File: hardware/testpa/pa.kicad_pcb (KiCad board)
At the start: 4 copper layers, 50 x 50 mm, 61 parts, among them CN1 CONN_01X02, J1 JNC, J2 JNC, Q1 LDMOS, Q2 LDMOS, T1 TRANSF4CTS, T2 1:1 Z, U1 LP2985

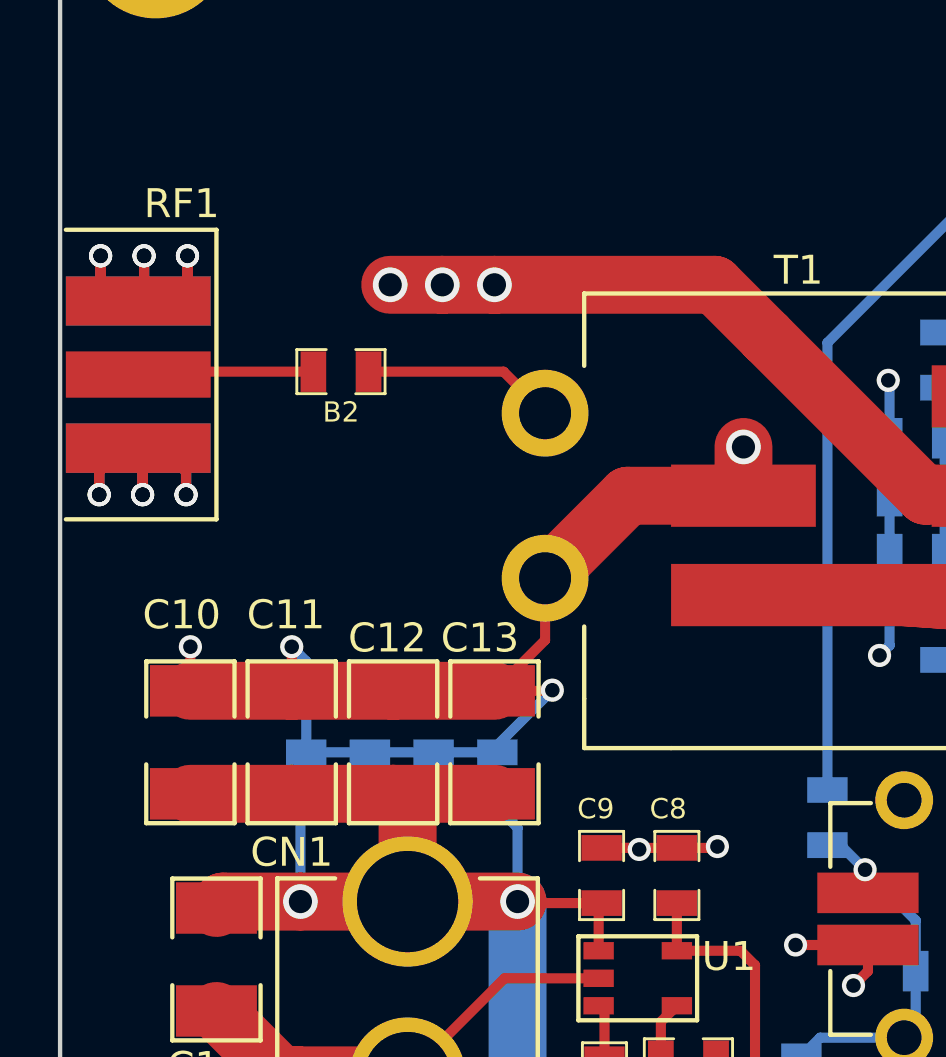
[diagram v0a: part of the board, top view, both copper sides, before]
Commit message: RF output fix on testpa
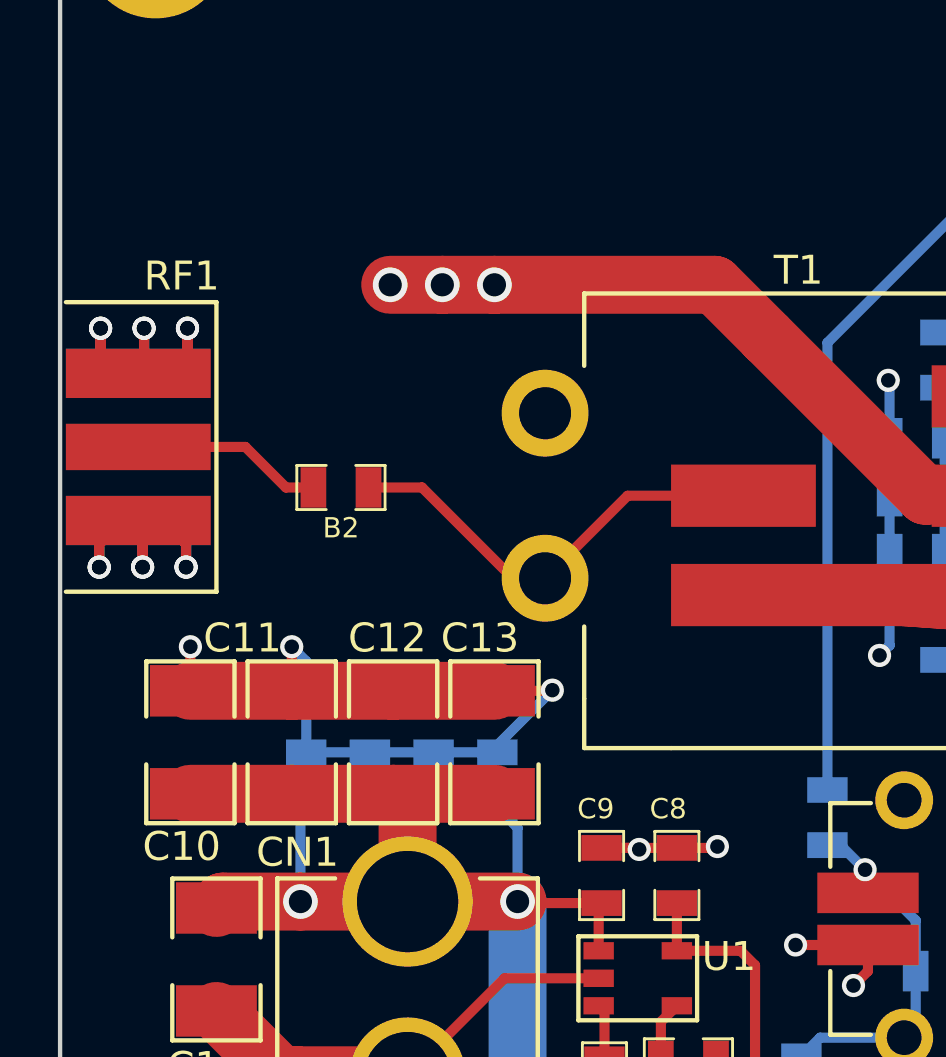
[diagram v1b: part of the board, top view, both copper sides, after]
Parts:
- moved B2 4.00 mm to (124.7, 97.0)
- moved RF1 2.50 mm to (115.0, 95.6)
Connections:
- T1 pad 4: Net-(B2-Pad2) -> GND
- T1 pad 5: GND -> Net-(B2-Pad2)
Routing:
- net GND: track 303.2 -> 288.6 mm, vias 57 -> 56
- net Net-(B2-Pad2): track 6.69 -> 15.4 mm
- net Net-(B2-Pad1): track 6.09 -> 6.63 mm

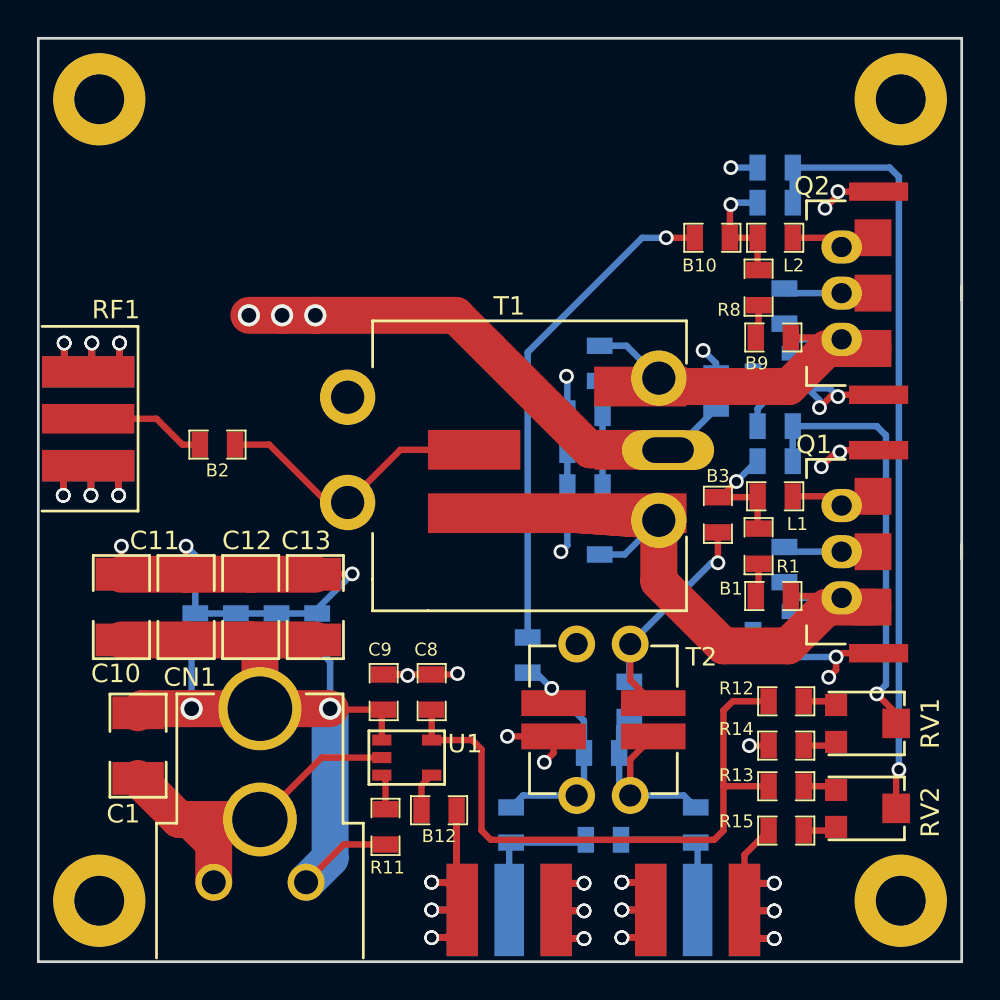
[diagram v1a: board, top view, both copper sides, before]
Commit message: Silk screen sizes, copyright notice
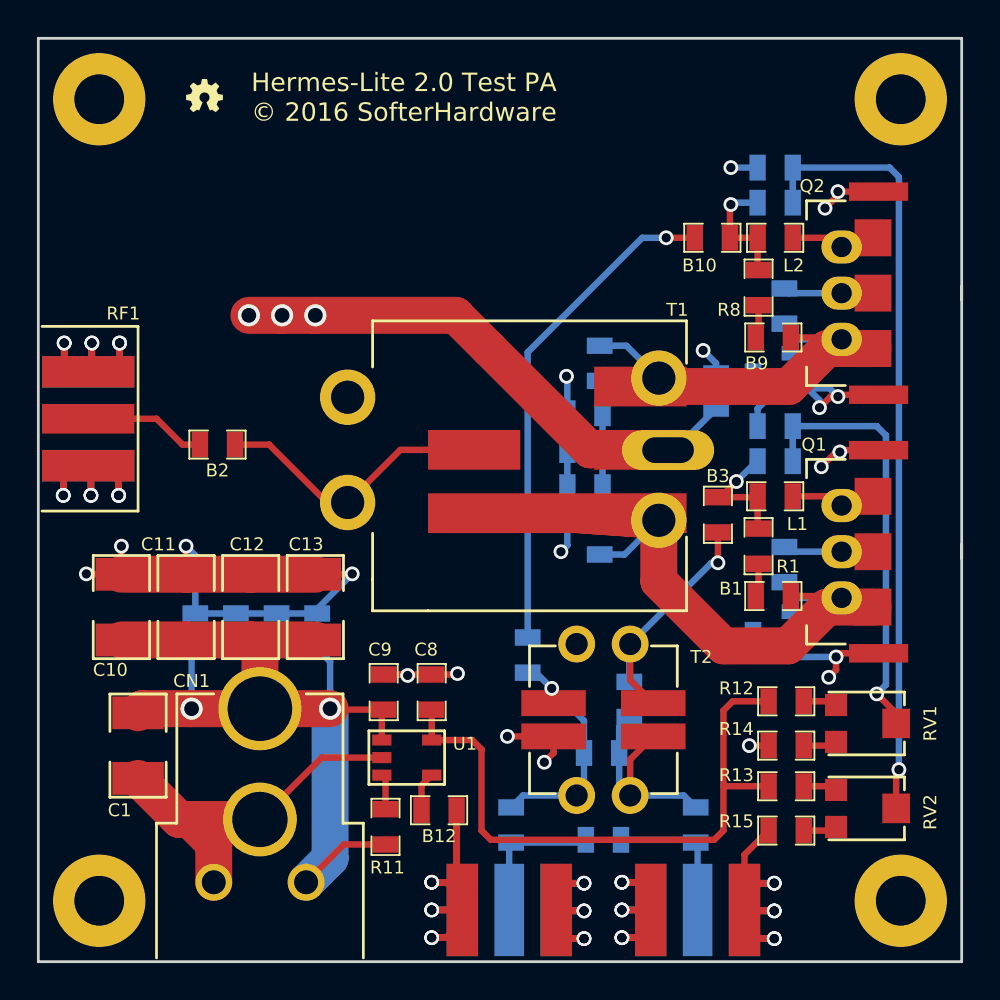
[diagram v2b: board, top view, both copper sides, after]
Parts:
- added G***: OSHW-logo_silkscreen-back_2mm, HERMESLITE:OSHW-logo_silkscreen-back_2mm, F.Cu at (124.0, 78.1)
- added G***: OSHW-logo_silkscreen-back_2mm, HERMESLITE:OSHW-logo_silkscreen-back_2mm, B.Cu at (124.0, 78.1)
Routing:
- net GND: track 288.6 -> 290.5 mm, vias 56 -> 57
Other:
- board text added: "Hermes-Lite 2.0 Test PA © 2016 SofterHardware"

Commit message: Final PCBs, added gerber
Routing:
- net /Vpa: track 147.2 -> 159.2 mm
- net GND: track 290.5 -> 302.3 mm, vias 57 -> 62
- net Net-(J2-Pad2): track 13.0 -> 16.1 mm
- added copper zone on B.Cu, net GND
- added copper zone on F.Cu, net GND
